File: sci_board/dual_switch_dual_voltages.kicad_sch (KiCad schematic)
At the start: 7 parts, among them U6 TPS22968QDMGRQ1

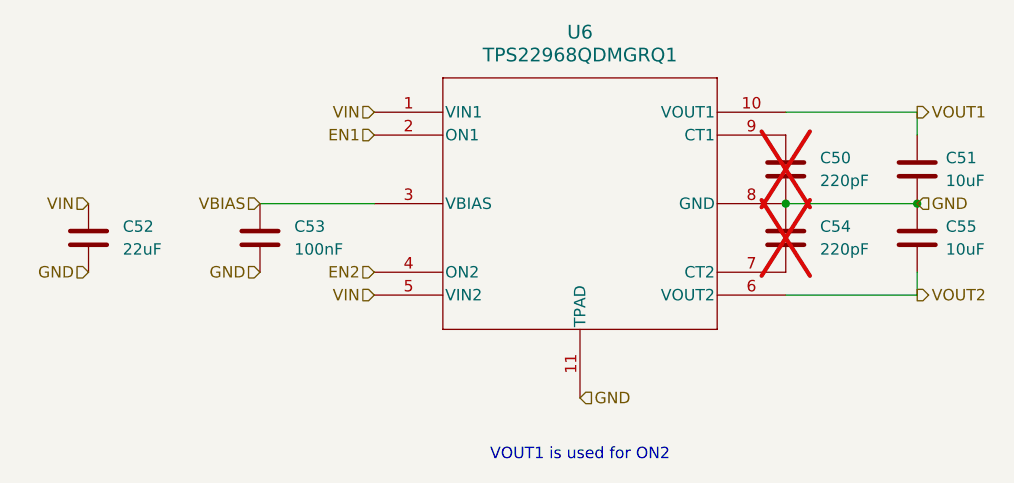
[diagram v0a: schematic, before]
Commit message: SCI AVI and EPS are consistent again
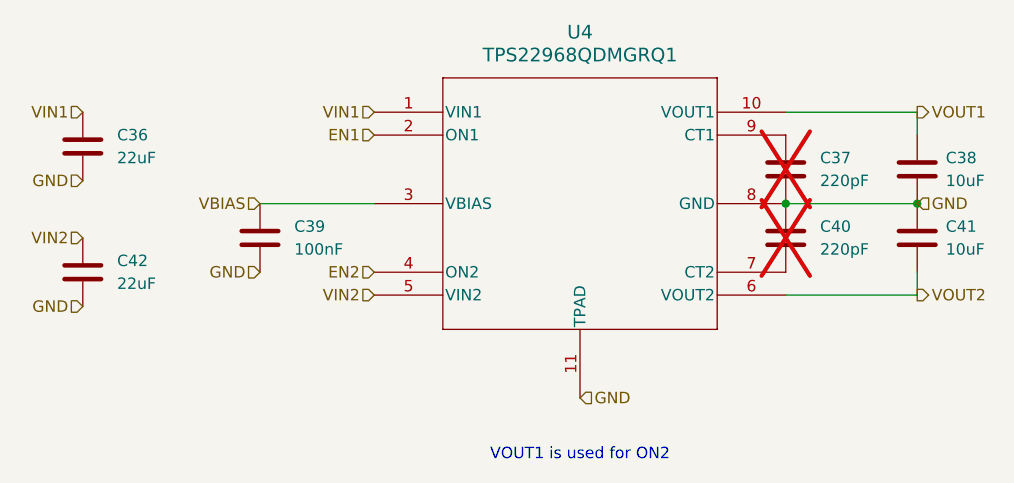
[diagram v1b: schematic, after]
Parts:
- removed C50, C54: 220pF, Capacitor_SMD:C_0402_1005Metric_Pad0.74x0.62mm_HandSolder, symbol Device:C
- removed C51, C55: 10uF, Capacitor_SMD:C_0603_1608Metric_Pad1.08x0.95mm_HandSolder, symbol Device:C
- removed C52: 22uF, Capacitor_SMD:C_0603_1608Metric_Pad1.08x0.95mm_HandSolder, symbol Device:C
- removed C53: 100nF, Capacitor_SMD:C_0402_1005Metric_Pad0.74x0.62mm_HandSolder, symbol Device:C
- removed U6: TPS22968QDMGRQ1, Package_SON:WSON-10-1EP_2x3mm_P0.5mm_EP0.84x2.4mm, symbol Common:TPS22968QDMGRQ1
- added C36, C42: 22uF, Capacitor_SMD:C_0603_1608Metric_Pad1.08x0.95mm_HandSolder, symbol Device:C
- added C37, C40: 220pF, Capacitor_SMD:C_0402_1005Metric_Pad0.74x0.62mm_HandSolder, symbol Device:C
- added C38, C41: 10uF, Capacitor_SMD:C_0603_1608Metric_Pad1.08x0.95mm_HandSolder, symbol Device:C
- added C39: 100nF, Capacitor_SMD:C_0402_1005Metric_Pad0.74x0.62mm_HandSolder, symbol Device:C
- added U4: TPS22968QDMGRQ1, Package_SON:WSON-10-1EP_2x3mm_P0.5mm_EP0.84x2.4mm, symbol Common:TPS22968QDMGRQ1
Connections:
- net EN1: now also U4.2 (ON1)
- net EN2: now also U4.4 (ON2)
- net GND: now also C36.2, C37.2, C38.2, C39.2, C40.1, C41.1, C42.2, U4.11 (TPAD), U4.8 (GND)
- net VBIAS: now also C39.1, U4.3 (VBIAS)
- net VOUT1: now also C38.1, U4.10 (VOUT1)
- net VOUT2: now also C41.2, U4.6 (VOUT2)
- new net: C40.2, U4.7 (CT2)
- new net: C37.1, U4.9 (CT1)
- new net VIN1: C36.1, U4.1 (VIN1)
- new net VIN2: C42.1, U4.5 (VIN2)

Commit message: bom for SCI
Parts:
- C36, C42: Part Number GRM188R61E106KA73D -> GRM188R61A226ME15D; Tolerance 10 -> 20; Voltage 25 -> 10
- C37, C40: Part Number (none) -> GRM1555C1H221JA01J
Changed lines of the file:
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@@
 			)
 		)
-		(property "Datasheet" "https://search.murata.co.jp/Ceramy/image/img/A01X/G101/ENG/GRT1555C1H221FA02-01.pdf"
+		(property "Datasheet" "https://search.murata.co.jp/Ceramy/image/img/A01X/G101/ENG/GRM1555C1H221JA01-01.pdf"
 			(at 170.18 109.22 0)
 			(effects
@@
 		)
 		(property "Manufacturer" "Murata"
+			(at 170.18 109.22 0)
+			(effects
+				(font
+					(size 1.27 1.27)
+				)
+				(hide yes)
+			)
+		)
+		(property "Part Number" "GRM1555C1H221JA01J"
 			(at 170.18 109.22 0)
 			(effects
@@
 				)
 			)
-			(project "sci_board"
+			(project "sci_board_wo_switches"
 				(path "/b4b2c88d-f6cd-4e60-862d-e21f68728580/5e5b27f8-7a4c-45d0-95f8-aff71797fcd3/494c050a-ddc6-4c7b-845c-e35cdf3b4f0e"
 					(reference "C102")
@@
 				)
 			)
-			(project "sci_board"
+			(project "sci_board_wo_switches"
 				(path "/b4b2c88d-f6cd-4e60-862d-e21f68728580/5e5b27f8-7a4c-45d0-95f8-aff71797fcd3/494c050a-ddc6-4c7b-845c-e35cdf3b4f0e"
 					(reference "C103")
@@
 			)
 		)
-		(property "Description" ""
+		(property "Description" "IC PWR SWITCH N-CHAN 1:1 10WSON"
 			(at 102.87 152.4 0)
 			(effects
@@
 				)
 			)
-			(project "sci_board"
+			(project "sci_board_wo_switches"
 				(path "/b4b2c88d-f6cd-4e60-862d-e21f68728580/5e5b27f8-7a4c-45d0-95f8-aff71797fcd3/494c050a-ddc6-4c7b-845c-e35cdf3b4f0e"
 					(reference "U28")
@@
 				)
 			)
-			(project "sci_board"
+			(project "sci_board_wo_switches"
 				(path "/b4b2c88d-f6cd-4e60-862d-e21f68728580/5e5b27f8-7a4c-45d0-95f8-aff71797fcd3/494c050a-ddc6-4c7b-845c-e35cdf3b4f0e"
 					(reference "C101")
@@
 				)
 			)
-			(project "sci_board"
+			(project "sci_board_wo_switches"
 				(path "/b4b2c88d-f6cd-4e60-862d-e21f68728580/5e5b27f8-7a4c-45d0-95f8-aff71797fcd3/494c050a-ddc6-4c7b-845c-e35cdf3b4f0e"
 					(reference "C100")
@@
 			)
 		)
-		(property "Datasheet" "https://search.murata.co.jp/Ceramy/image/img/A01X/G101/ENG/GRM188R61E106KA73-01.pdf"
+		(property "Datasheet" "https://search.murata.co.jp/Ceramy/image/img/A01X/G101/ENG/GRM188R61A226ME15-01.pdf"
 			(at 92.075 99.06 0)
 			(effects
@@
 			)
 		)
-		(property "Tolerance" "10"
+		(property "Tolerance" "20"
 			(at 92.075 99.06 0)
 			(effects
@@
 			)
 		)
-		(property "Voltage" "25"
+		(property "Voltage" "10"
 			(at 92.075 99.06 0)
 			(effects
@@
 			)
 		)
-		(property "Part Number" "GRM188R61E106KA73D"
+		(property "Part Number" "GRM188R61A226ME15D"
 			(at 92.075 99.06 0)
 			(effects
@@
 				)
 			)
-			(project "sci_board"
+			(project "sci_board_wo_switches"
 				(path "/b4b2c88d-f6cd-4e60-862d-e21f68728580/5e5b27f8-7a4c-45d0-95f8-aff71797fcd3/494c050a-ddc6-4c7b-845c-e35cdf3b4f0e"
 					(reference "C98")
@@
 			)
 		)
-		(property "Datasheet" "https://search.murata.co.jp/Ceramy/image/img/A01X/G101/ENG/GRT1555C1H221FA02-01.pdf"
+		(property "Datasheet" "https://search.murata.co.jp/Ceramy/image/img/A01X/G101/ENG/GRM1555C1H221JA01-01.pdf"
 			(at 170.18 101.6 0)
 			(effects
@@
 		)
 		(property "Manufacturer" "Murata"
+			(at 170.18 101.6 0)
+			(effects
+				(font
+					(size 1.27 1.27)
+				)
+				(hide yes)
+			)
+		)
+		(property "Part Number" "GRM1555C1H221JA01J"
 			(at 170.18 101.6 0)
 			(effects
@@
 				)
 			)
-			(project "sci_board"
+			(project "sci_board_wo_switches"
 				(path "/b4b2c88d-f6cd-4e60-862d-e21f68728580/5e5b27f8-7a4c-45d0-95f8-aff71797fcd3/494c050a-ddc6-4c7b-845c-e35cdf3b4f0e"
 					(reference "C99")
@@
 			)
 		)
-		(property "Datasheet" "https://search.murata.co.jp/Ceramy/image/img/A01X/G101/ENG/GRM188R61E106KA73-01.pdf"
+		(property "Datasheet" "https://search.murata.co.jp/Ceramy/image/img/A01X/G101/ENG/GRM188R61A226ME15-01.pdf"
 			(at 92.075 113.03 0)
 			(effects
@@
 			)
 		)
-		(property "Tolerance" "10"
+		(property "Tolerance" "20"
 			(at 92.075 113.03 0)
 			(effects
@@
 			)
 		)
-		(property "Voltage" "25"
+		(property "Voltage" "10"
 			(at 92.075 113.03 0)
 			(effects
@@
 			)
 		)
-		(property "Part Number" "GRM188R61E106KA73D"
+		(property "Part Number" "GRM188R61A226ME15D"
 			(at 92.075 113.03 0)
 			(effects
@@
 		)
 		(instances
-			(project "sci_board"
+			(project "sci_board_wo_switches"
 				(path "/b4b2c88d-f6cd-4e60-862d-e21f68728580/5e5b27f8-7a4c-45d0-95f8-aff71797fcd3/494c050a-ddc6-4c7b-845c-e35cdf3b4f0e"
 					(reference "C104")

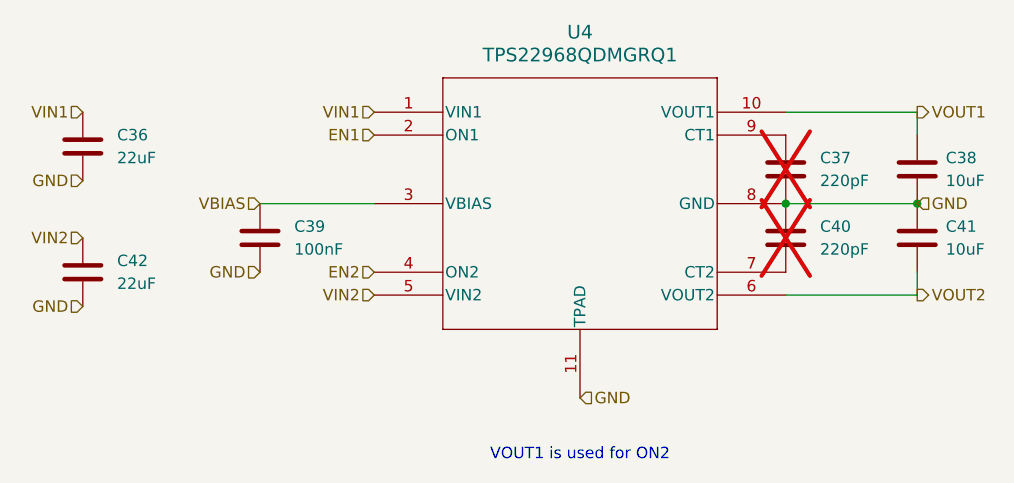
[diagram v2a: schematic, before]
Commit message: sorting out pullups on resets and attention. replace reset with RN where possible. Introduce CN to save some parts
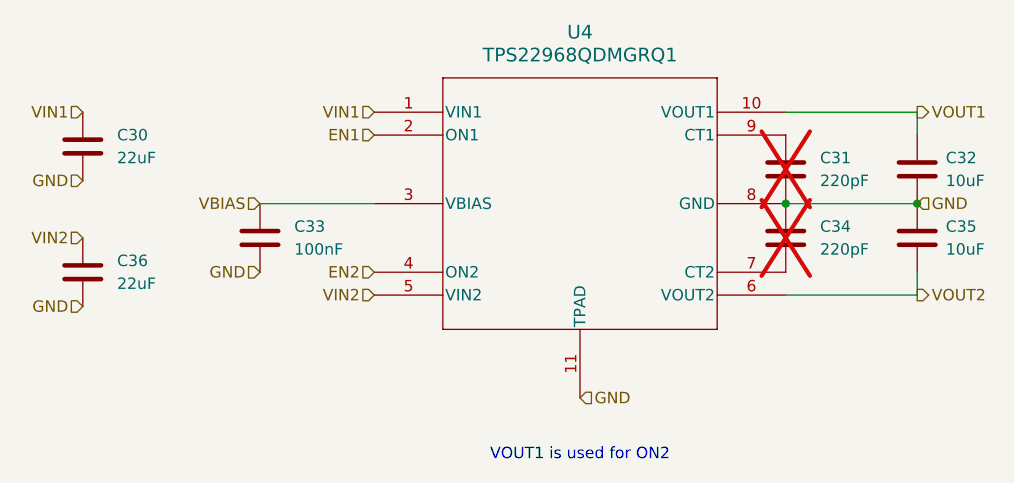
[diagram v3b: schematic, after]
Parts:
- renumbered C36 to C30, C37 to C31, C38 to C32, C39 to C33, C40 to C34, C41 to C35, C42 to C36
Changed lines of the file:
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@@
 		(dnp yes)
 		(fields_autoplaced yes)
-		(property "Reference" "C40"
+		(property "Reference" "C34"
 			(at 173.99 107.9499 0)
 			(effects
@@
 			(project "sci_board_wo_switches"
 				(path "/b4b2c88d-f6cd-4e60-862d-e21f68728580/5e5b27f8-7a4c-45d0-95f8-aff71797fcd3/494c050a-ddc6-4c7b-845c-e35cdf3b4f0e"
-					(reference "C102")
+					(reference "C85")
 					(unit 1)
 				)
 				(path "/b4b2c88d-f6cd-4e60-862d-e21f68728580/5e5b27f8-7a4c-45d0-95f8-aff71797fcd3/4f83ada3-39c3-49cb-bc7e-b35233b0e659"
-					(reference "C40")
+					(reference "C34")
 					(unit 1)
 				)
 				(path "/b4b2c88d-f6cd-4e60-862d-e21f68728580/5e5b27f8-7a4c-45d0-95f8-aff71797fcd3/8ef13ba3-4aa4-4ee3-bfa2-75083ef40e6c"
-					(reference "C47")
+					(reference "C41")
 					(unit 1)
 				)
@@
 		(dnp no)
 		(fields_autoplaced yes)
-		(property "Reference" "C41"
+		(property "Reference" "C35"
 			(at 187.96 107.9499 0)
 			(effects
@@
 			(project "sci_board_wo_switches"
 				(path "/b4b2c88d-f6cd-4e60-862d-e21f68728580/5e5b27f8-7a4c-45d0-95f8-aff71797fcd3/494c050a-ddc6-4c7b-845c-e35cdf3b4f0e"
-					(reference "C103")
+					(reference "C86")
 					(unit 1)
 				)
 				(path "/b4b2c88d-f6cd-4e60-862d-e21f68728580/5e5b27f8-7a4c-45d0-95f8-aff71797fcd3/4f83ada3-39c3-49cb-bc7e-b35233b0e659"
-					(reference "C41")
+					(reference "C35")
 					(unit 1)
 				)
 				(path "/b4b2c88d-f6cd-4e60-862d-e21f68728580/5e5b27f8-7a4c-45d0-95f8-aff71797fcd3/8ef13ba3-4aa4-4ee3-bfa2-75083ef40e6c"
-					(reference "C48")
+					(reference "C42")
 					(unit 1)
 				)
@@
 				(font
 					(size 1.27 1.27)
-					(italic yes)
 				)
 				(hide yes)
@@
 				(font
 					(size 1.27 1.27)
-					(italic yes)
 				)
 				(hide yes)
@@
 			(project "sci_board_wo_switches"
 				(path "/b4b2c88d-f6cd-4e60-862d-e21f68728580/5e5b27f8-7a4c-45d0-95f8-aff71797fcd3/494c050a-ddc6-4c7b-845c-e35cdf3b4f0e"
-					(reference "U28")
+					(reference "U19")
 					(unit 1)
 				)
@@
 		(dnp no)
 		(fields_autoplaced yes)
-		(property "Reference" "C39"
+		(property "Reference" "C33"
 			(at 115.57 107.9499 0)
 			(effects
@@
 			(project "sci_board_wo_switches"
 				(path "/b4b2c88d-f6cd-4e60-862d-e21f68728580/5e5b27f8-7a4c-45d0-95f8-aff71797fcd3/494c050a-ddc6-4c7b-845c-e35cdf3b4f0e"
-					(reference "C101")
+					(reference "C84")
 					(unit 1)
 				)
 				(path "/b4b2c88d-f6cd-4e60-862d-e21f68728580/5e5b27f8-7a4c-45d0-95f8-aff71797fcd3/4f83ada3-39c3-49cb-bc7e-b35233b0e659"
-					(reference "C39")
+					(reference "C33")
 					(unit 1)
 				)
 				(path "/b4b2c88d-f6cd-4e60-862d-e21f68728580/5e5b27f8-7a4c-45d0-95f8-aff71797fcd3/8ef13ba3-4aa4-4ee3-bfa2-75083ef40e6c"
-					(reference "C46")
+					(reference "C40")
 					(unit 1)
 				)
@@
 		(dnp no)
 		(fields_autoplaced yes)
-		(property "Reference" "C38"
+		(property "Reference" "C32"
 			(at 187.96 100.3299 0)
 			(effects
@@
 			(project "sci_board_wo_switches"
 				(path "/b4b2c88d-f6cd-4e60-862d-e21f68728580/5e5b27f8-7a4c-45d0-95f8-aff71797fcd3/494c050a-ddc6-4c7b-845c-e35cdf3b4f0e"
-					(reference "C100")
+					(reference "C83")
 					(unit 1)
 				)
 				(path "/b4b2c88d-f6cd-4e60-862d-e21f68728580/5e5b27f8-7a4c-45d0-95f8-aff71797fcd3/4f83ada3-39c3-49cb-bc7e-b35233b0e659"
-					(reference "C38")
+					(reference "C32")
 					(unit 1)
 				)
 				(path "/b4b2c88d-f6cd-4e60-862d-e21f68728580/5e5b27f8-7a4c-45d0-95f8-aff71797fcd3/8ef13ba3-4aa4-4ee3-bfa2-75083ef40e6c"
-					(reference "C45")
+					(reference "C39")
 					(unit 1)
 				)
@@
 		(dnp no)
 		(fields_autoplaced yes)
-		(property "Reference" "C36"
+		(property "Reference" "C30"
 			(at 95.885 97.7899 0)
 			(effects
@@
 			(project "sci_board_wo_switches"
 				(path "/b4b2c88d-f6cd-4e60-862d-e21f68728580/5e5b27f8-7a4c-45d0-95f8-aff71797fcd3/494c050a-ddc6-4c7b-845c-e35cdf3b4f0e"
-					(reference "C98")
+					(reference "C81")
 					(unit 1)
 				)
 				(path "/b4b2c88d-f6cd-4e60-862d-e21f68728580/5e5b27f8-7a4c-45d0-95f8-aff71797fcd3/4f83ada3-39c3-49cb-bc7e-b35233b0e659"
-					(reference "C36")
+					(reference "C30")
 					(unit 1)
 				)
 				(path "/b4b2c88d-f6cd-4e60-862d-e21f68728580/5e5b27f8-7a4c-45d0-95f8-aff71797fcd3/8ef13ba3-4aa4-4ee3-bfa2-75083ef40e6c"
-					(reference "C43")
+					(reference "C37")
 					(unit 1)
 				)
@@
 		(dnp yes)
 		(fields_autoplaced yes)
-		(property "Reference" "C37"
+		(property "Reference" "C31"
 			(at 173.99 100.3299 0)
 			(effects
@@
 			(project "sci_board_wo_switches"
 				(path "/b4b2c88d-f6cd-4e60-862d-e21f68728580/5e5b27f8-7a4c-45d0-95f8-aff71797fcd3/494c050a-ddc6-4c7b-845c-e35cdf3b4f0e"
-					(reference "C99")
+					(reference "C82")
 					(unit 1)
 				)
 				(path "/b4b2c88d-f6cd-4e60-862d-e21f68728580/5e5b27f8-7a4c-45d0-95f8-aff71797fcd3/4f83ada3-39c3-49cb-bc7e-b35233b0e659"
-					(reference "C37")
+					(reference "C31")
 					(unit 1)
 				)
 				(path "/b4b2c88d-f6cd-4e60-862d-e21f68728580/5e5b27f8-7a4c-45d0-95f8-aff71797fcd3/8ef13ba3-4aa4-4ee3-bfa2-75083ef40e6c"
-					(reference "C44")
+					(reference "C38")
 					(unit 1)
 				)
@@
 		(dnp no)
 		(fields_autoplaced yes)
-		(property "Reference" "C42"
+		(property "Reference" "C36"
 			(at 95.885 111.7599 0)
 			(effects
@@
 			(project "sci_board_wo_switches"
 				(path "/b4b2c88d-f6cd-4e60-862d-e21f68728580/5e5b27f8-7a4c-45d0-95f8-aff71797fcd3/494c050a-ddc6-4c7b-845c-e35cdf3b4f0e"
-					(reference "C104")
+					(reference "C87")
 					(unit 1)
 				)
 				(path "/b4b2c88d-f6cd-4e60-862d-e21f68728580/5e5b27f8-7a4c-45d0-95f8-aff71797fcd3/4f83ada3-39c3-49cb-bc7e-b35233b0e659"
-					(reference "C42")
+					(reference "C36")
 					(unit 1)
 				)
 				(path "/b4b2c88d-f6cd-4e60-862d-e21f68728580/5e5b27f8-7a4c-45d0-95f8-aff71797fcd3/8ef13ba3-4aa4-4ee3-bfa2-75083ef40e6c"
-					(reference "C49")
-					(unit 1)
-				)
+					(reference "C43")
+					(unit 1)
+				)

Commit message: checked BOM for sci wo switches
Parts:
- C31, C34: Tolerance 1 -> 5
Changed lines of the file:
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@@
 			)
 		)
-		(property "Tolerance" "1"
+		(property "Tolerance" "5"
 			(at 170.18 109.22 0)
 			(effects
@@
 			(project "sci_board_wo_switches"
 				(path "/b4b2c88d-f6cd-4e60-862d-e21f68728580/5e5b27f8-7a4c-45d0-95f8-aff71797fcd3/494c050a-ddc6-4c7b-845c-e35cdf3b4f0e"
-					(reference "C102")
+					(reference "C85")
 					(unit 1)
 				)
@@
 			(project "sci_board_wo_switches"
 				(path "/b4b2c88d-f6cd-4e60-862d-e21f68728580/5e5b27f8-7a4c-45d0-95f8-aff71797fcd3/494c050a-ddc6-4c7b-845c-e35cdf3b4f0e"
-					(reference "C103")
+					(reference "C86")
 					(unit 1)
 				)
@@
 			(project "sci_board_wo_switches"
 				(path "/b4b2c88d-f6cd-4e60-862d-e21f68728580/5e5b27f8-7a4c-45d0-95f8-aff71797fcd3/494c050a-ddc6-4c7b-845c-e35cdf3b4f0e"
-					(reference "U28")
+					(reference "U19")
 					(unit 1)
 				)
@@
 			(project "sci_board_wo_switches"
 				(path "/b4b2c88d-f6cd-4e60-862d-e21f68728580/5e5b27f8-7a4c-45d0-95f8-aff71797fcd3/494c050a-ddc6-4c7b-845c-e35cdf3b4f0e"
-					(reference "C101")
+					(reference "C84")
 					(unit 1)
 				)
@@
 			(project "sci_board_wo_switches"
 				(path "/b4b2c88d-f6cd-4e60-862d-e21f68728580/5e5b27f8-7a4c-45d0-95f8-aff71797fcd3/494c050a-ddc6-4c7b-845c-e35cdf3b4f0e"
-					(reference "C100")
+					(reference "C83")
 					(unit 1)
 				)
@@
 			(project "sci_board_wo_switches"
 				(path "/b4b2c88d-f6cd-4e60-862d-e21f68728580/5e5b27f8-7a4c-45d0-95f8-aff71797fcd3/494c050a-ddc6-4c7b-845c-e35cdf3b4f0e"
-					(reference "C98")
+					(reference "C81")
 					(unit 1)
 				)
@@
 			)
 		)
-		(property "Tolerance" "1"
+		(property "Tolerance" "5"
 			(at 170.18 101.6 0)
 			(effects
@@
 			(project "sci_board_wo_switches"
 				(path "/b4b2c88d-f6cd-4e60-862d-e21f68728580/5e5b27f8-7a4c-45d0-95f8-aff71797fcd3/494c050a-ddc6-4c7b-845c-e35cdf3b4f0e"
-					(reference "C99")
+					(reference "C82")
 					(unit 1)
 				)
@@
 			(project "sci_board_wo_switches"
 				(path "/b4b2c88d-f6cd-4e60-862d-e21f68728580/5e5b27f8-7a4c-45d0-95f8-aff71797fcd3/494c050a-ddc6-4c7b-845c-e35cdf3b4f0e"
-					(reference "C104")
-					(unit 1)
-				)
+					(reference "C87")
+					(unit 1)
+				)
